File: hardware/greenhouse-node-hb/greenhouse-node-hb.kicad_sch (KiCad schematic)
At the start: 39 parts, among them J1 Conn_01x02_Pin, J4 Conn_01x02_Pin, J5 Conn_01x04_Pin, SW1 SW_Push, U1 XC6706x, U3 PCF8574ATS/3,118, U5 L7810, U6 STM32F030F4P6, U7 RFM69HW, U8 A4952ELYTR-T

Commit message: Finish PCB for TS, and renamed boards
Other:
- title: Greenhouse Node Mini -> Greenhouse Node HB (Mini)

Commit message: Tweaks to nodes
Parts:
- added D8: BAT46, Diode_THT:D_DO-35_SOD27_P7.62mm_Horizontal, symbol Diode:BAT46
- added J2: Conn_01x03, Jumper:SolderJumper-3_P1.3mm_Bridged2Bar12_RoundedPad1.0x1.5mm, symbol Connector_Generic:Conn_01x03
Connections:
- net +10V: now also D8.2 (A); no longer D1.2 (A)
- net at C1.2, U1.3 (IN): now also J2.2 (Pin_2); no longer D1.1 (K)
- net +12V: now reaches C4.2, J4.1 (Pin_1), U5.1 (IN)
- net +12V: now also D1.2 (A)
- new net: D1.1 (K), J2.1 (Pin_1)
- new net: D8.1 (K), J2.3 (Pin_3)
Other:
- moved on the sheet: AE1, C1, C10, C2, C3, C4, C5, C6, C7, C9, D2, D3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

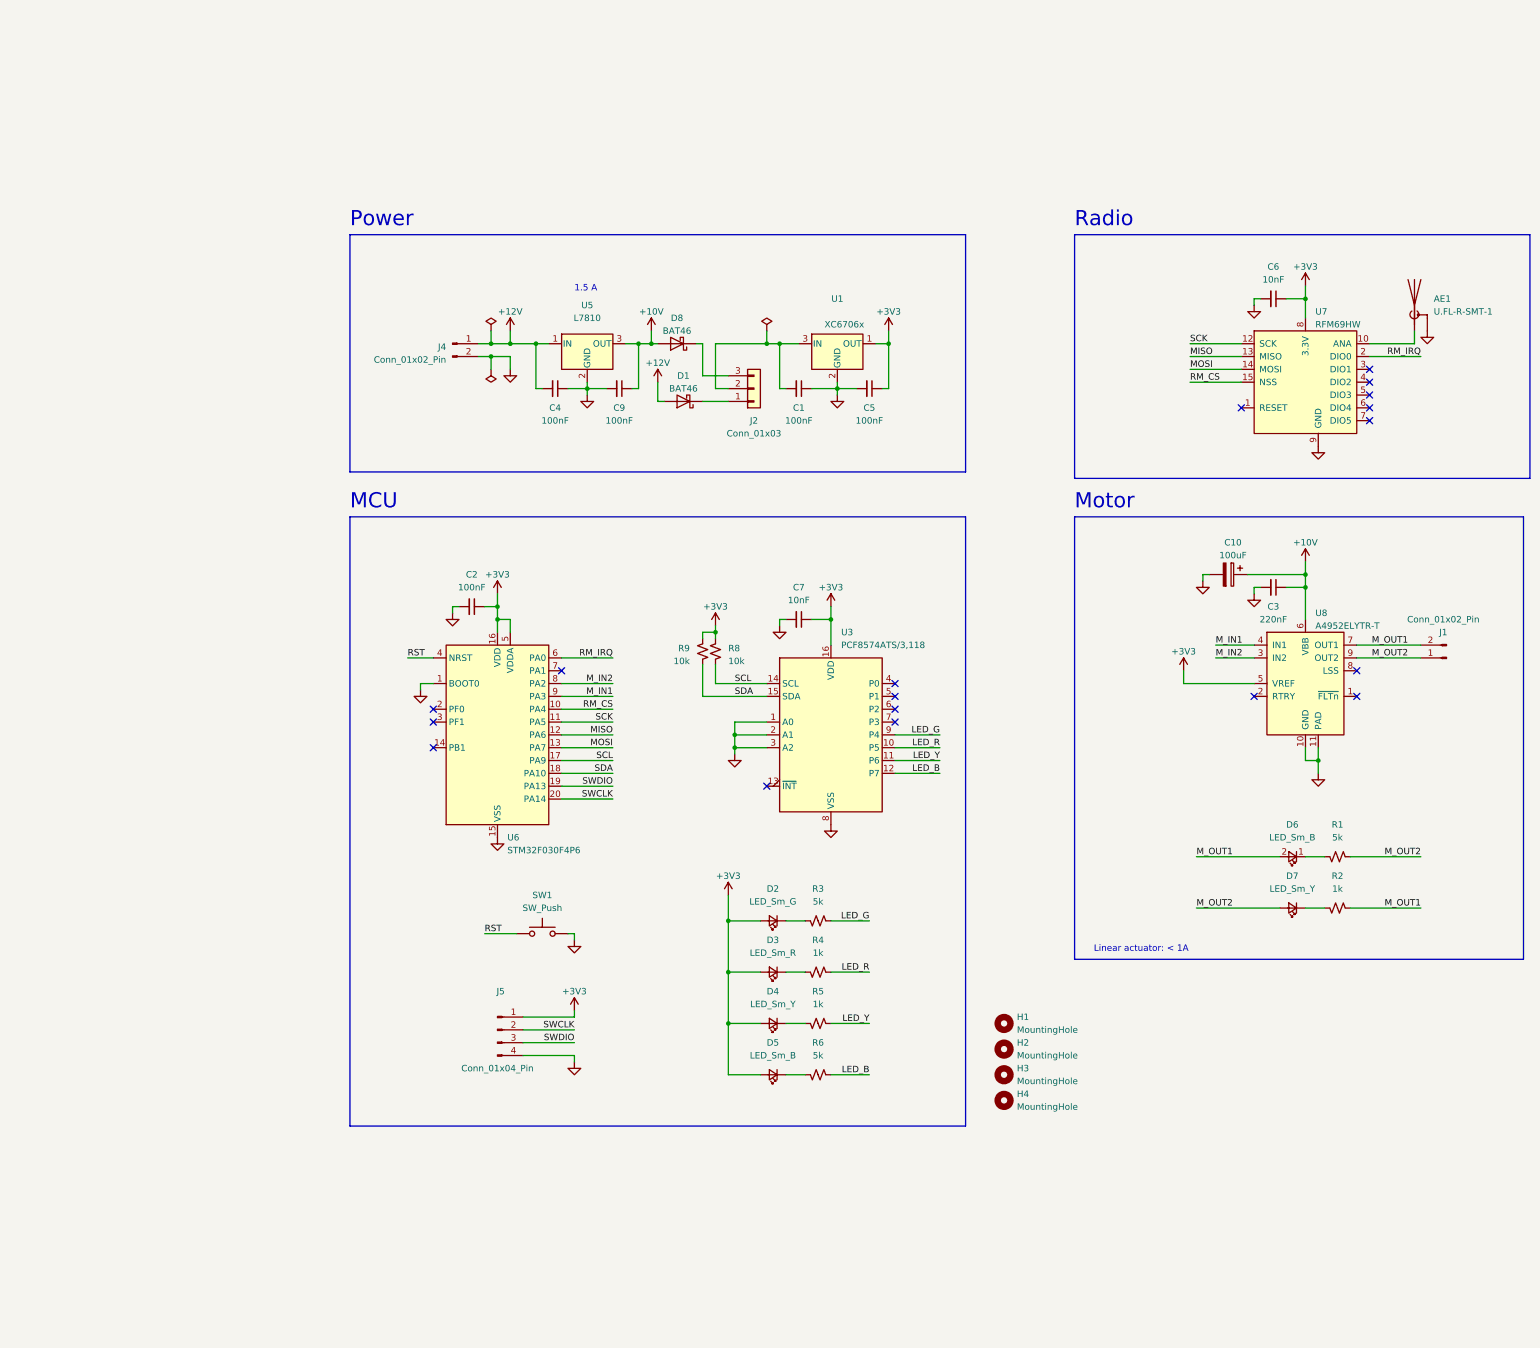
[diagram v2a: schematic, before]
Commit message: Fixed cap sizes, generated BOMs
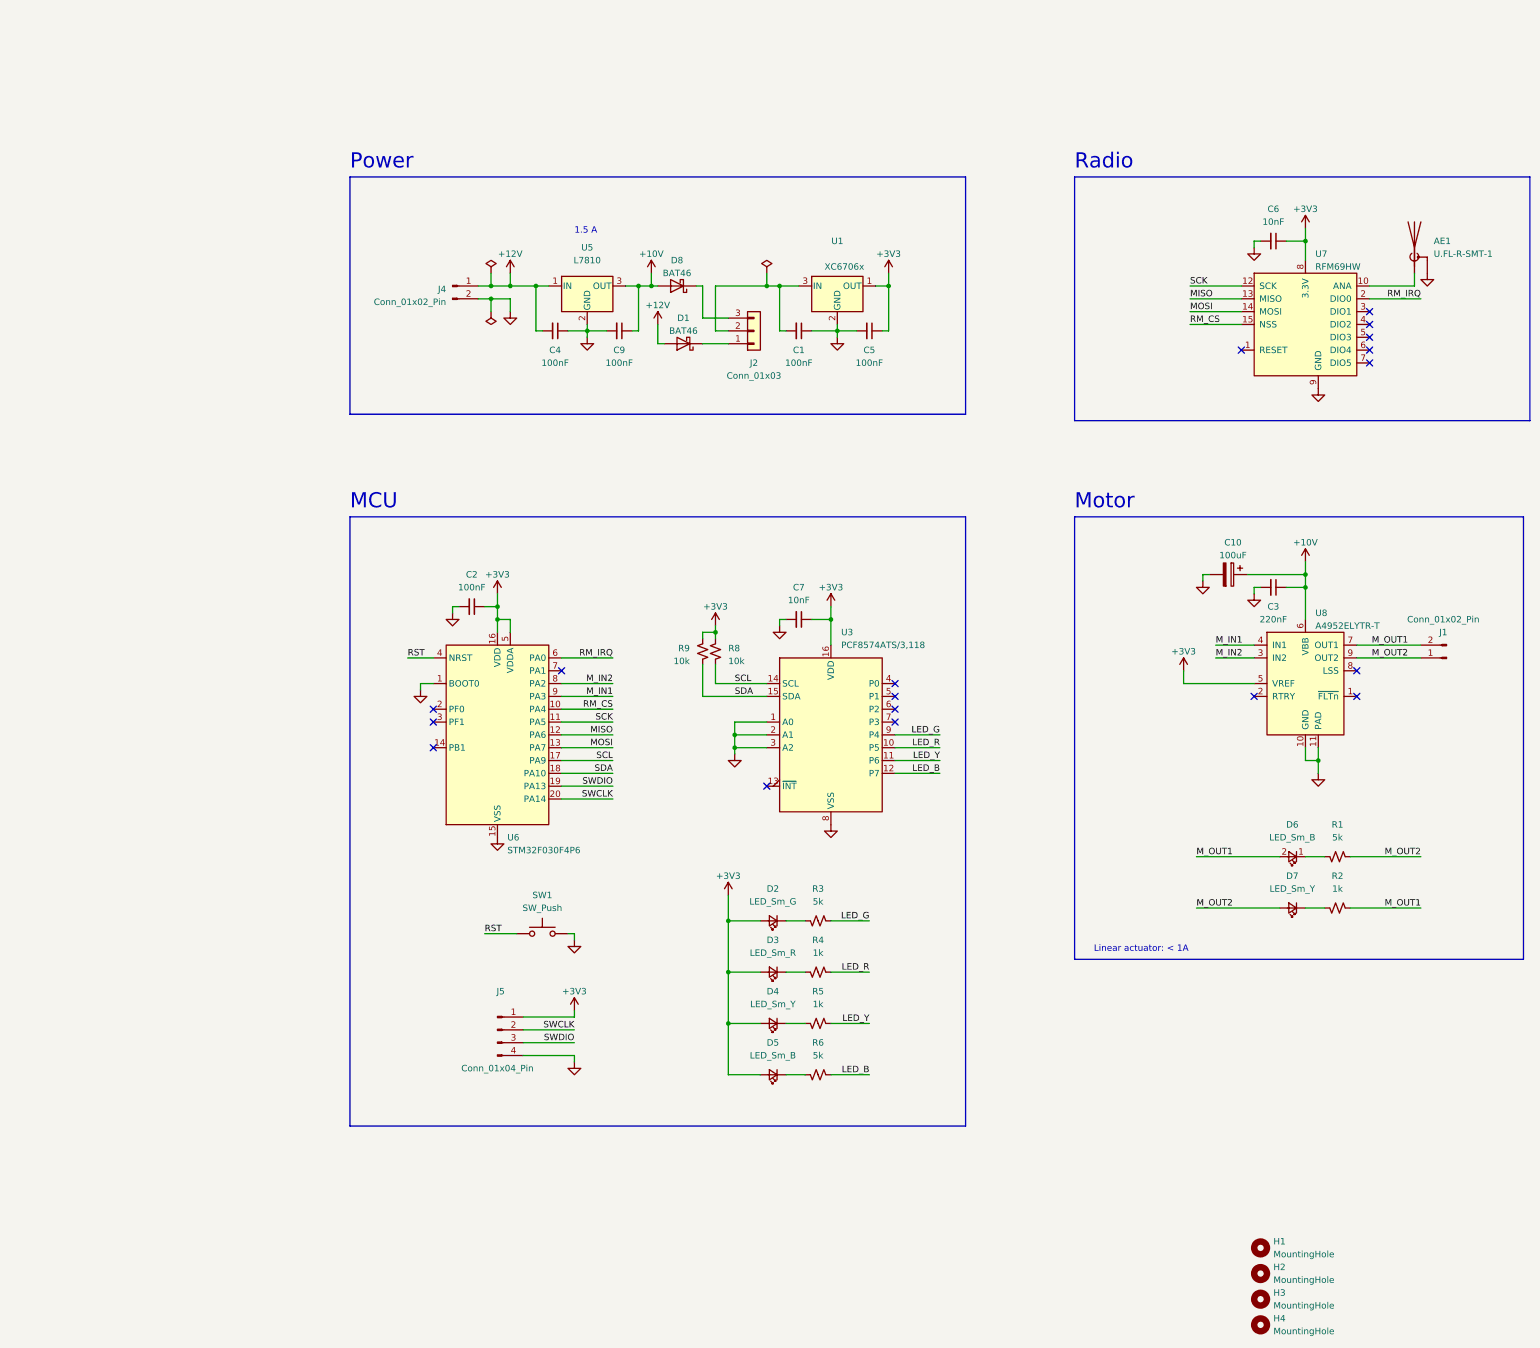
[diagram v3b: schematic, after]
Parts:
- C6, C7: footprint Capacitor_THT:C_Disc_D4.7mm_W2.5mm_P5.00mm -> Capacitor_THT:C_Disc_D3.0mm_W2.0mm_P2.50mm
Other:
- moved on the sheet: AE1, C1, C4, C5, C6, C9, D1, D8, H1, H2, H3, H4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

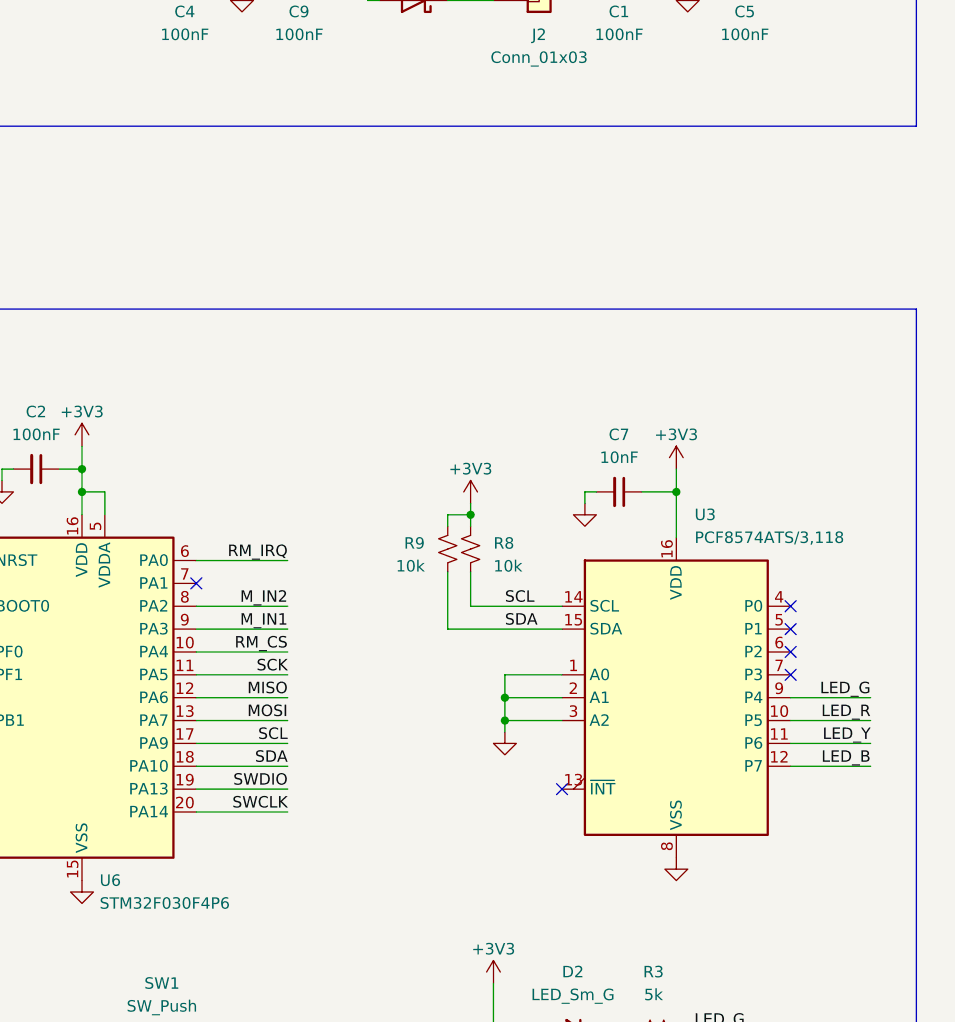
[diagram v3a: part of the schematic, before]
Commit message: Improved schematics
Add todos, test points, fixed PCF8574 symbol,
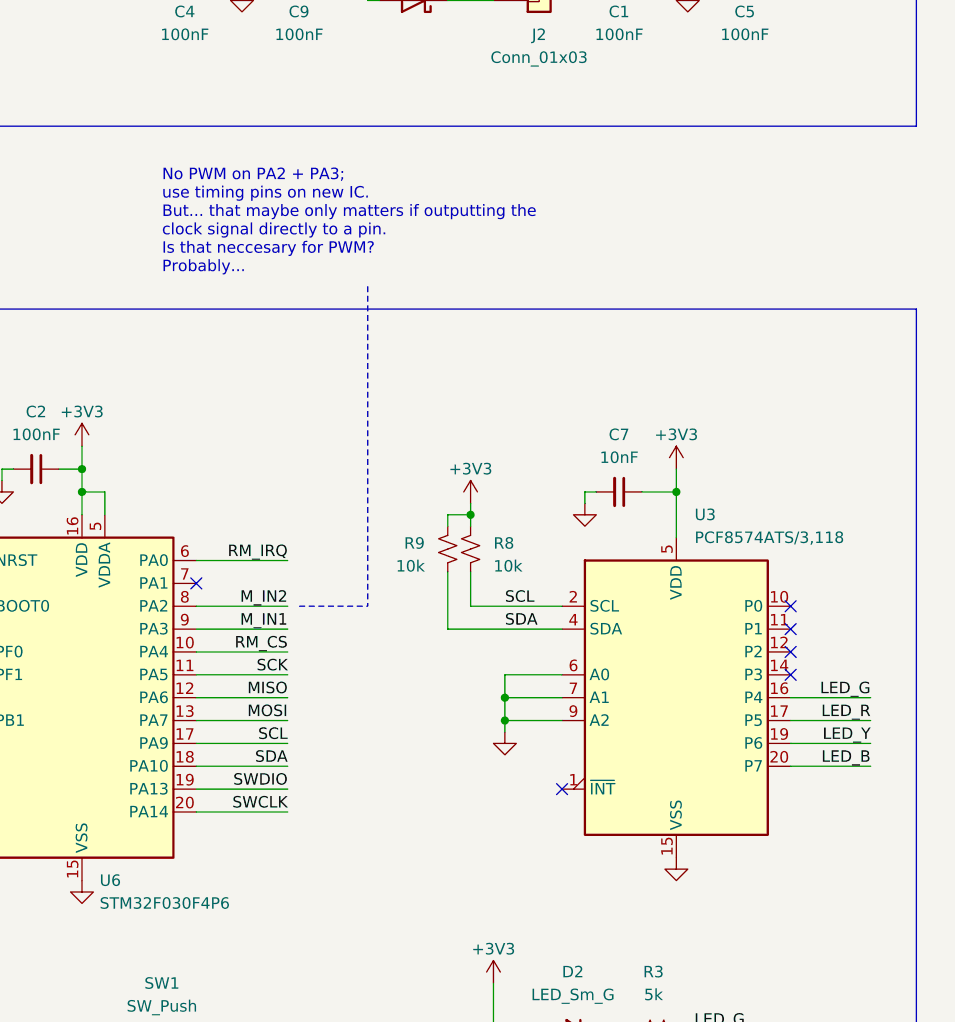
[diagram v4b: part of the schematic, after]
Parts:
- U3: symbol Interface_Expansion:PCF8574 -> Interface_Expansion:PCF8574ATS
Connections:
- net +3V3: now also U3.5 (VDD); no longer U3.16 (VDD)
- net GND: now also U3.15 (VSS), U3.6 (A0), U3.7 (A1), U3.9 (A2); no longer U3.1 (A0), U3.2 (A1), U3.3 (A2), U3.8 (VSS)
- net LED_B: now also U3.20 (P7); no longer U3.12 (P7)
- net LED_G: now also U3.16 (P4); no longer U3.9 (P4)
- net LED_R: now also U3.17 (P5); no longer U3.10 (P5)
- net LED_Y: now also U3.19 (P6); no longer U3.11 (P6)
- net SCL: now also U3.2 (SCL); no longer U3.14 (SCL)
- net SDA: now also U3.4 (SDA); no longer U3.15 (SDA)
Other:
- note added: "No PWM on PA2 + PA3; use timing pins on new IC. But... that maybe only matters if outputting the clock signal directly to a pin. Is that neccesary for PWM? Probably..."
